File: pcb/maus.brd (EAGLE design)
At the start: 100 x 100 mm, 85 parts, among them IC1 AP1509-50SG-13, J1 SS-52300-001, Q2 BSS123, Q3 BSS123, Q4 BSS123, Q6 PMN30XPEAHEATSINK, Q7 PMN30XPEAHEATSINK, U1 ESP32-S2-WROOM, U2 CH340C, U4 LP3965EMP-3.3, U5 LSM9DS1TR, U6 LM358DR

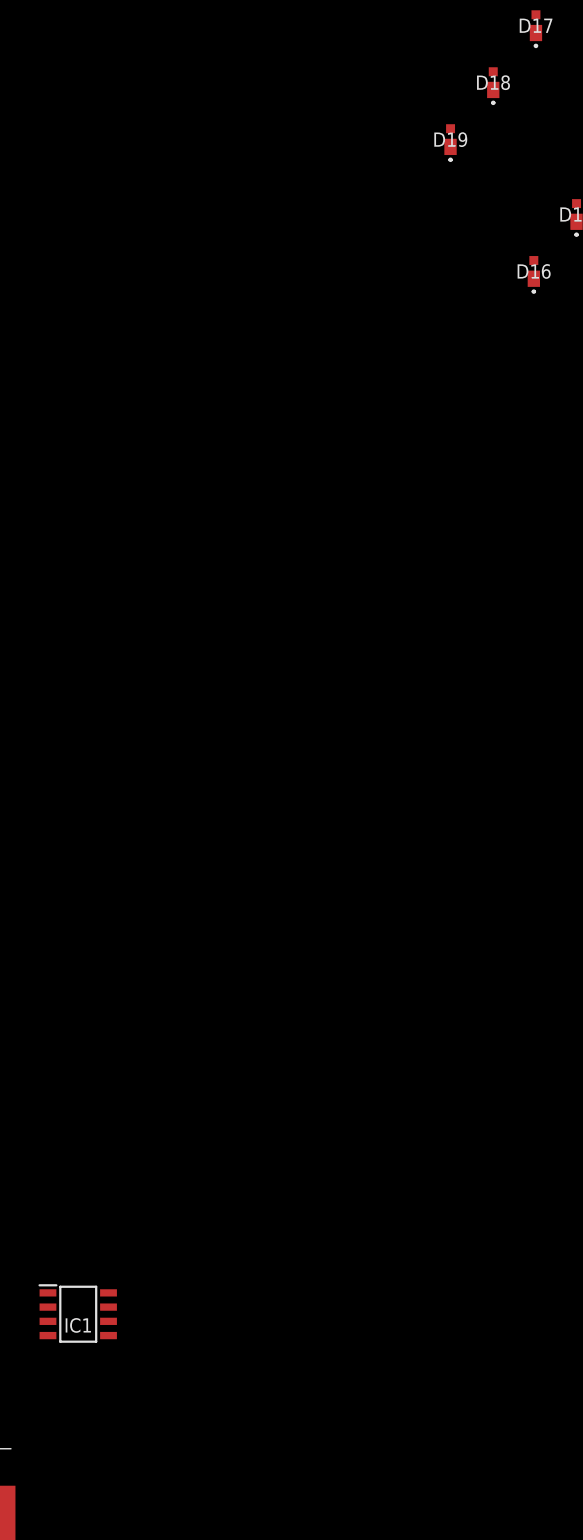
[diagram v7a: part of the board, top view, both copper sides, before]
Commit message: fixed some ERC errors
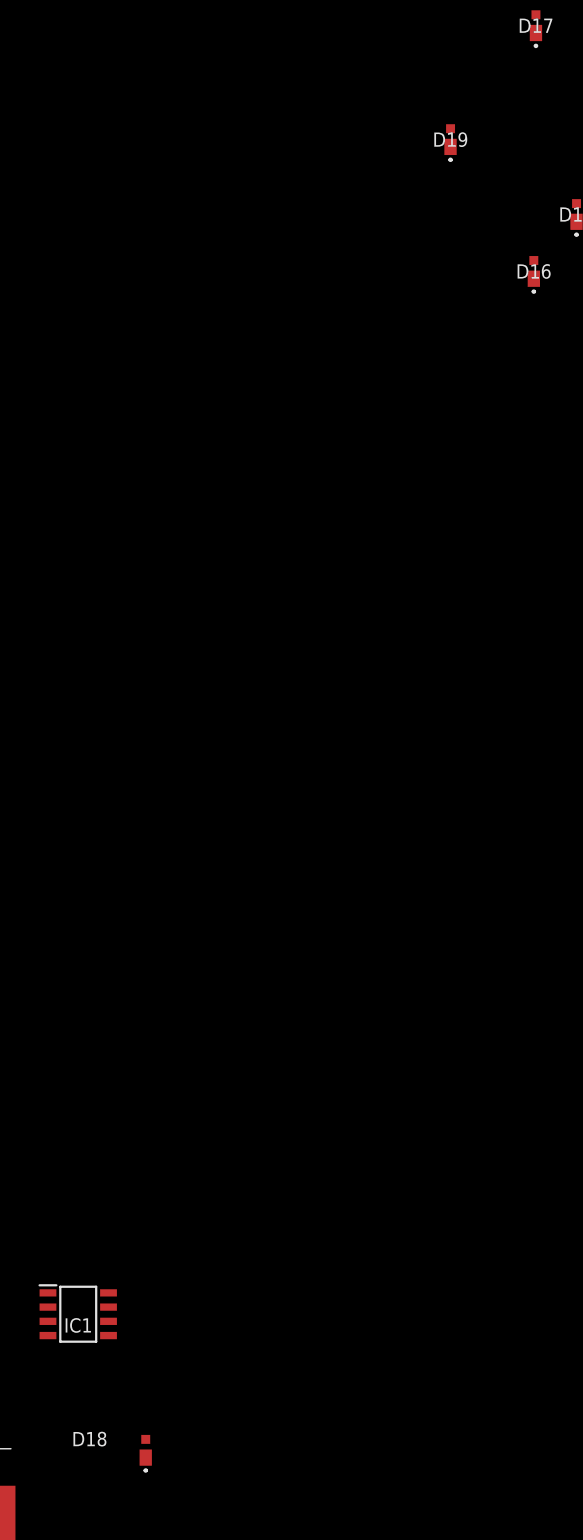
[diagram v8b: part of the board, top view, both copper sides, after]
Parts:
- moved D18 125.9 mm to (-98.0, -102.1)
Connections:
- removed net IO7: JP5.10
- net GND: now also D18.2
- net M2_M+: now also D18.1
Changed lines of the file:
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@@
 <attribute name="VALUE" x="-63.17" y="24.94" size="1.27" layer="27" align="center"/>
 </element>
-<element name="D18" library="shared" package="RB068VWM100" value="RBR2VWM40ATF" x="-66.98" y="19.86" smashed="yes">
-<attribute name="ARROW_PART_NUMBER" value="" x="-66.98" y="19.86" size="1.778" layer="27" display="off"/>
-<attribute name="ARROW_PRICE-STOCK" value="" x="-66.98" y="19.86" size="1.778" layer="27" display="off"/>
-<attribute name="DESCRIPTION" value="Low V&lt;sub&gt;F&lt;/sub&gt;, 40V, 2A, Schottky Barrier Diode for Automoive" x="-66.98" y="19.86" size="1.778" layer="27" display="off"/>
-<attribute name="HEIGHT" value="0.95mm" x="-66.98" y="19.86" size="1.778" layer="27" display="off"/>
-<attribute name="MANUFACTURER_NAME" value="ROHM Semiconductor" x="-66.98" y="19.86" size="1.778" layer="27" display="off"/>
-<attribute name="MANUFACTURER_PART_NUMBER" value="RBR2VWM40ATF" x="-66.98" y="19.86" size="1.778" layer="27" display="off"/>
-<attribute name="MOUSER_PART_NUMBER" value="" x="-66.98" y="19.86" size="1.778" layer="27" display="off"/>
-<attribute name="MOUSER_PRICE-STOCK" value="" x="-66.98" y="19.86" size="1.778" layer="27" display="off"/>
-<attribute name="NAME" x="-66.98" y="19.86" size="1.27" layer="25" align="center"/>
-<attribute name="VALUE" x="-66.98" y="19.86" size="1.27" layer="27" align="center"/>
+<element name="D18" library="shared" package="RB068VWM100" value="RBR2VWM40ATF" x="-97.98" y="-102.14" smashed="yes">
+<attribute name="ARROW_PART_NUMBER" value="" x="-97.98" y="-102.14" size="1.778" layer="27" display="off"/>
+<attribute name="ARROW_PRICE-STOCK" value="" x="-97.98" y="-102.14" size="1.778" layer="27" display="off"/>
+<attribute name="DESCRIPTION" value="Low V&lt;sub&gt;F&lt;/sub&gt;, 40V, 2A, Schottky Barrier Diode for Automoive" x="-97.98" y="-102.14" size="1.778" layer="27" display="off"/>
+<attribute name="HEIGHT" value="0.95mm" x="-97.98" y="-102.14" size="1.778" layer="27" display="off"/>
+<attribute name="MANUFACTURER_NAME" value="ROHM Semiconductor" x="-97.98" y="-102.14" size="1.778" layer="27" display="off"/>
+<attribute name="MANUFACTURER_PART_NUMBER" value="RBR2VWM40ATF" x="-97.98" y="-102.14" size="1.778" layer="27" display="off"/>
+<attribute name="MOUSER_PART_NUMBER" value="" x="-97.98" y="-102.14" size="1.778" layer="27" display="off"/>
+<attribute name="MOUSER_PRICE-STOCK" value="" x="-97.98" y="-102.14" size="1.778" layer="27" display="off"/>
+<attribute name="NAME" x="-102.98" y="-101.14" size="1.27" layer="25" align="center"/>
+<attribute name="VALUE" x="-97.98" y="-102.14" size="1.27" layer="27" align="center"/>
 </element>
 <element name="D19" library="shared" package="RB068VWM100" value="RBR2VWM40ATF" x="-70.79" y="14.78" smashed="yes">
@@
 <contactref element="C12" pad="2"/>
 <contactref element="R2" pad="1"/>
+<contactref element="D18" pad="2"/>
 <wire x1="-122" y1="-133.025" x2="-123.05" y2="-128" width="0" layer="19" extent="1-1"/>
 <wire x1="-123.05" y1="-121" x2="-123.05" y2="-128" width="0" layer="19" extent="1-1"/>
 <wire x1="-126.05" y1="-140" x2="-122" y2="-133.025" width="0" layer="19" extent="1-1"/>
 <wire x1="-127.95" y1="-147" x2="-126.05" y2="-140" width="0" layer="19" extent="1-1"/>
-<wire x1="-101.3" y1="-91.905" x2="-123.05" y2="-121" width="0" layer="19" extent="1-1"/>
+<wire x1="-97.98" y1="-101.165" x2="-123.05" y2="-121" width="0" layer="19" extent="1-1"/>
+<wire x1="-101.3" y1="-91.905" x2="-97.98" y2="-101.165" width="0" layer="19" extent="1-1"/>
 <wire x1="-101.3" y1="-90.635" x2="-101.3" y2="-91.905" width="0" layer="19" extent="1-1"/>
 <wire x1="-101.3" y1="-89.365" x2="-101.3" y2="-90.635" width="0" layer="19" extent="1-1"/>
 <wire x1="-101.3" y1="-88.095" x2="-101.3" y2="-89.365" width="0" layer="19" extent="1-1"/>
-<wire x1="-70.79" y1="15.755" x2="-101.3" y2="-88.095" width="0" layer="19" extent="1-1"/>
-<wire x1="-59.55" y1="9.075" x2="-70.79" y2="15.755" width="0" layer="19" extent="1-1"/>
+<wire x1="-59.55" y1="9.075" x2="-101.3" y2="-88.095" width="0" layer="19" extent="1-1"/>
 <wire x1="-55.74" y1="14.155" x2="-59.55" y2="9.075" width="0" layer="19" extent="1-1"/>
-<wire x1="20.64" y1="36.83" x2="-55.74" y2="14.155" width="0" layer="19" extent="1-1"/>
-<wire x1="18.5674" y1="41.91" x2="20.64" y2="36.83" width="0" layer="19" extent="1-1"/>
+<wire x1="-70.79" y1="15.755" x2="-59.55" y2="9.075" width="0" layer="19" extent="1-1"/>
+<wire x1="18.5674" y1="41.91" x2="-55.74" y2="14.155" width="0" layer="19" extent="1-1"/>
 <wire x1="20.64" y1="46.99" x2="18.5674" y2="41.91" width="0" layer="19" extent="1-1"/>
+<wire x1="20.64" y1="36.83" x2="18.5674" y2="41.91" width="0" layer="19" extent="1-1"/>
 <wire x1="38.735" y1="30.4778" x2="20.64" y2="36.83" width="0" layer="19" extent="1-1"/>
 <wire x1="40.005" y1="30.4778" x2="38.735" y2="30.4778" width="0" layer="19" extent="1-1"/>
@@
 <wire x1="76.06" y1="28.13" x2="76.2" y2="80.01" width="0" layer="19" extent="1-1"/>
 </signal>
-<signal name="IO7">
-<contactref element="JP5" pad="10"/>
-</signal>
 <signal name="D_N">
 <contactref element="D1" pad="3"/>
@@
 <wire x1="-111.05" y1="-108" x2="-124.95" y2="-121" width="0" layer="19" extent="1-1"/>
 <wire x1="-106.7" y1="-90.635" x2="-111.05" y2="-108" width="0" layer="19" extent="1-1"/>
-<wire x1="22.54" y1="36.83" x2="-111.05" y2="-108" width="0" layer="19" extent="1-1"/>
+<wire x1="22.54" y1="36.83" x2="-106.7" y2="-90.635" width="0" layer="19" extent="1-1"/>
 <wire x1="24.6126" y1="41.148" x2="22.54" y2="36.83" width="0" layer="19" extent="1-1"/>
 <wire x1="33.34" y1="40.64" x2="24.6126" y2="41.148" width="0" layer="19" extent="1-1"/>
@@
 <contactref element="IC1" pad="1"/>
 <contactref element="C12" pad="1"/>
-<wire x1="-63.17" y1="24.29" x2="-106.7" y2="-88.095" width="0" layer="19" extent="1-1"/>
-<wire x1="-63.36" y1="2.37" x2="-63.17" y2="24.29" width="0" layer="19" extent="1-1"/>
+<wire x1="-127.95" y1="-140" x2="-106.7" y2="-88.095" width="0" layer="19" extent="1-1"/>
+<wire x1="-63.36" y1="2.37" x2="-106.7" y2="-88.095" width="0" layer="19" extent="1-1"/>
 <wire x1="-51.93" y1="17.61" x2="-63.36" y2="2.37" width="0" layer="19" extent="1-1"/>
 <wire x1="-48.12" y1="22.69" x2="-51.93" y2="17.61" width="0" layer="19" extent="1-1"/>
-<wire x1="-127.95" y1="-140" x2="-106.7" y2="-88.095" width="0" layer="19" extent="1-1"/>
+<wire x1="-63.17" y1="24.29" x2="-51.93" y2="17.61" width="0" layer="19" extent="1-1"/>
 <wire x1="31.96" y1="19.05" x2="-48.12" y2="22.69" width="0" layer="19" extent="1-1"/>
 <wire x1="43.18" y1="24.45" x2="31.96" y2="19.05" width="0" layer="19" extent="1-1"/>
@@
 <contactref element="CR1" pad="16"/>
 <contactref element="D16" pad="2"/>
+<contactref element="D18" pad="1"/>
+<wire x1="-63.36" y1="3.995" x2="-97.98" y2="-102.79" width="0" layer="19" extent="1-1"/>
 <wire x1="22.86" y1="64.77" x2="-63.36" y2="3.995" width="0" layer="19" extent="1-1"/>
 <wire x1="74.0156" y1="51.435" x2="22.86" y2="64.77" width="0" layer="19" extent="1-1"/>
@@
 <contactref element="D17" pad="2"/>
 <contactref element="D19" pad="1"/>
-<wire x1="-63.17" y1="25.915" x2="-70.79" y2="14.13" width="0" layer="19" extent="1-1"/>
-<wire x1="20.32" y1="64.77" x2="-63.17" y2="25.915" width="0" layer="19" extent="1-1"/>
-<wire x1="74.0156" y1="52.705" x2="20.32" y2="64.77" width="0" layer="19" extent="1-1"/>
+<wire x1="20.32" y1="64.77" x2="74.0156" y2="52.705" width="0" layer="19" extent="1-1"/>
+<wire x1="-63.17" y1="25.915" x2="20.32" y2="64.77" width="0" layer="19" extent="1-1"/>
+<wire x1="-70.79" y1="14.13" x2="-63.17" y2="25.915" width="0" layer="19" extent="1-1"/>
 </signal>
 <signal name="/VBUS_EN">
